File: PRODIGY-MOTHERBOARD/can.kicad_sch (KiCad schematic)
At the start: 10 parts, among them U4 TJA1051T-E

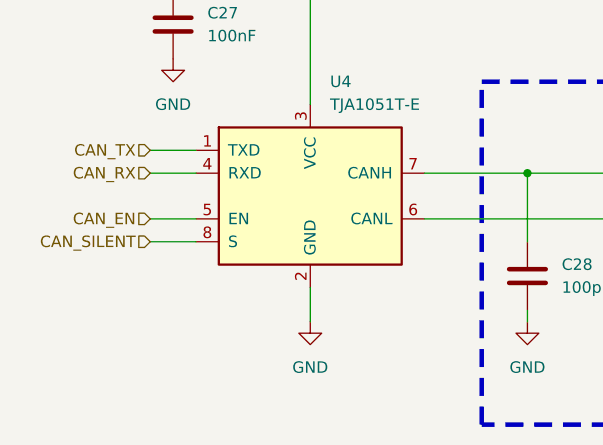
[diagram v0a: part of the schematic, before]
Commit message: MBT Schematic improved
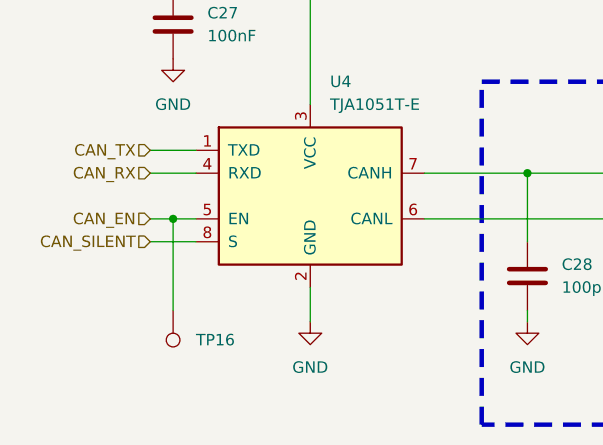
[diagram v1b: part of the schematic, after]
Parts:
- added TP16: ~, TestPoint:TestPoint_Pad_D3.0mm, symbol Connector:TestPoint
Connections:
- net CAN_EN: now also TP16.1
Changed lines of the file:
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@@
+	)
+	(junction
+		(at 95.25 91.44)
+		(diameter 0)
+		(color 0 0 0 0)
 	)
 	(junction
@@
 	(wire
 		(pts
+			(xy 95.25 91.44) (xy 95.25 101.6)
+		)
+		(stroke
+			(width 0)
+			(type default)
+		)
+	)
+	(wire
+		(pts
 			(xy 210.82 80.01) (xy 248.92 80.01)
 		)
@@
 	(wire
 		(pts
+			(xy 95.25 91.44) (xy 97.79 91.44)
+		)
+		(stroke
+			(width 0)
+			(type default)
+		)
+	)
+	(wire
+		(pts
 			(xy 110.49 66.04) (xy 110.49 78.74)
 		)
@@
 	(wire
 		(pts
-			(xy 92.71 91.44) (xy 97.79 91.44)
+			(xy 92.71 91.44) (xy 95.25 91.44)
 		)
 		(stroke
@@
 					(unit 1)
 				)
+			)
+		)
+	)
+	(symbol
+		(lib_id "Connector:TestPoint")
+		(at 95.25 101.6 180)
+		(unit 1)
+		(exclude_from_sim no)
+		(in_bom no)
+		(on_board yes)
+		(dnp no)
+		(fields_autoplaced yes)
+		(property "Reference" "TP16"
+			(at 97.79 104.9019 0)
+			(effects
+				(font
+					(size 1.27 1.27)
+				)
+				(justify right)
+			)
+		)
+		(property "Value" "~"
+			(at 92.71 102.997 0)
+			(effects
+				(font
+					(size 1.27 1.27)
+				)
+				(justify left)
+				(hide yes)
+			)
+		)
+		(property "Footprint" "TestPoint:TestPoint_Pad_D3.0mm"
+			(at 90.17 101.6 0)
+			(effects
+				(font
+					(size 1.27 1.27)
+				)
+				(hide yes)
+			)
+		)
+		(property "Datasheet" "~"
+			(at 90.17 101.6 0)
+			(effects
+				(font
+					(size 1.27 1.27)
+				)
+				(hide yes)
+			)
+		)
+		(property "Description" ""
+			(at 95.25 101.6 0)
+			(effects
+				(font
+					(size 1.27 1.27)
+				)
+				(hide yes)
+			)
+		)
+		(pin "1"
+		)
+		(instances
+			(project "PRODIGY-MOTHERBOARD"
+				(path "/f1c25860-8989-4190-bd24-2491d23ca7d9/cf0d8bf1-4632-49df-9398-b3de35528304"
+					(reference "TP16")
+					(unit 1)
+				)

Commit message: schematic v0.2 finalized
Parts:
- added FID11, FID12: Fiducial, symbol Mechanical:Fiducial
- renumbered C27 to C26, C28 to C27, C29 to C28, C30 to C29, C31 to C30, C32 to C31, TP16 to TP9
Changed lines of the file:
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@@
 		(dnp no)
 		(fields_autoplaced yes)
-		(property "Reference" "#PWR064"
+		(property "Reference" "#PWR067"
 			(at 220.98 105.41 0)
 			(effects
@@
 			(project "PRODIGY-MOTHERBOARD"
 				(path "/f1c25860-8989-4190-bd24-2491d23ca7d9/cf0d8bf1-4632-49df-9398-b3de35528304"
-					(reference "#PWR064")
+					(reference "#PWR067")
 					(unit 1)
 				)
@@
 		(dnp no)
 		(fields_autoplaced yes)
-		(property "Reference" "TP16"
+		(property "Reference" "TP9"
 			(at 97.79 104.9019 0)
 			(effects
@@
 			(project "PRODIGY-MOTHERBOARD"
 				(path "/f1c25860-8989-4190-bd24-2491d23ca7d9/cf0d8bf1-4632-49df-9398-b3de35528304"
-					(reference "TP16")
+					(reference "TP9")
 					(unit 1)
 				)
@@
 		(dnp no)
 		(fields_autoplaced yes)
-		(property "Reference" "C29"
+		(property "Reference" "C28"
 			(at 152.4 96.5199 0)
 			(effects
@@
 			(project "PRODIGY-MOTHERBOARD"
 				(path "/f1c25860-8989-4190-bd24-2491d23ca7d9/cf0d8bf1-4632-49df-9398-b3de35528304"
-					(reference "C29")
+					(reference "C28")
 					(unit 1)
 				)
@@
 		(dnp no)
 		(fields_autoplaced yes)
-		(property "Reference" "#PWR063"
+		(property "Reference" "#PWR066"
 			(at 180.34 109.22 0)
 			(effects
@@
 			(project "PRODIGY-MOTHERBOARD"
 				(path "/f1c25860-8989-4190-bd24-2491d23ca7d9/cf0d8bf1-4632-49df-9398-b3de35528304"
-					(reference "#PWR063")
+					(reference "#PWR066")
 					(unit 1)
 				)
@@
 		(dnp no)
 		(fields_autoplaced yes)
-		(property "Reference" "#PWR061"
+		(property "Reference" "#PWR064"
 			(at 148.59 109.22 0)
 			(effects
@@
 			(project "PRODIGY-MOTHERBOARD"
 				(path "/f1c25860-8989-4190-bd24-2491d23ca7d9/cf0d8bf1-4632-49df-9398-b3de35528304"
-					(reference "#PWR061")
+					(reference "#PWR064")
+					(unit 1)
+				)
+			)
+		)
+	)
+	(symbol
+		(lib_id "Mechanical:Fiducial")
+		(at 133.35 121.92 0)
+		(unit 1)
+		(exclude_from_sim no)
+		(in_bom yes)
+		(on_board yes)
+		(dnp no)
+		(fields_autoplaced yes)
+		(property "Reference" "FID11"
+			(at 135.89 120.6499 0)
+			(effects
+				(font
+					(size 1.27 1.27)
+				)
+				(justify left)
+			)
+		)
+		(property "Value" "Fiducial"
+			(at 135.89 123.1899 0)
+			(effects
+				(font
+					(size 1.27 1.27)
+				)
+				(justify left)
+			)
+		)
+		(property "Footprint" ""
+			(at 133.35 121.92 0)
+			(effects
+				(font
+					(size 1.27 1.27)
+				)
+				(hide yes)
+			)
+		)
+		(property "Datasheet" "~"
+			(at 133.35 121.92 0)
+			(effects
+				(font
+					(size 1.27 1.27)
+				)
+				(hide yes)
+			)
+		)
+		(property "Description" "Fiducial Marker"
+			(at 133.35 121.92 0)
+			(effects
+				(font
+					(size 1.27 1.27)
+				)
+				(hide yes)
+			)
+		)
+		(instances
+			(project "PRODIGY-MOTHERBOARD"
+				(path "/f1c25860-8989-4190-bd24-2491d23ca7d9/cf0d8bf1-4632-49df-9398-b3de35528304"
+					(reference "FID11")
 					(unit 1)
 				)
@@
 		(dnp no)
 		(fields_autoplaced yes)
-		(property "Reference" "C32"
+		(property "Reference" "C31"
 			(at 224.79 91.4399 0)
 			(effects
@@
 			(project "PRODIGY-MOTHERBOARD"
 				(path "/f1c25860-8989-4190-bd24-2491d23ca7d9/cf0d8bf1-4632-49df-9398-b3de35528304"
-					(reference "C32")
+					(reference "C31")
 					(unit 1)
 				)
@@
 		(dnp no)
 		(fields_autoplaced yes)
-		(property "Reference" "#PWR062"
+		(property "Reference" "#PWR065"
 			(at 166.37 109.22 0)
 			(effects
@@
 			(project "PRODIGY-MOTHERBOARD"
 				(path "/f1c25860-8989-4190-bd24-2491d23ca7d9/cf0d8bf1-4632-49df-9398-b3de35528304"
-					(reference "#PWR062")
+					(reference "#PWR065")
 					(unit 1)
 				)
@@
 		(dnp no)
 		(fields_autoplaced yes)
-		(property "Reference" "C28"
+		(property "Reference" "C27"
 			(at 138.43 96.5199 0)
 			(effects
@@
 			(project "PRODIGY-MOTHERBOARD"
 				(path "/f1c25860-8989-4190-bd24-2491d23ca7d9/cf0d8bf1-4632-49df-9398-b3de35528304"
-					(reference "C28")
+					(reference "C27")
 					(unit 1)
 				)
@@
 		(dnp no)
 		(fields_autoplaced yes)
-		(property "Reference" "#PWR060"
+		(property "Reference" "#PWR063"
 			(at 134.62 109.22 0)
 			(effects
@@
 			(project "PRODIGY-MOTHERBOARD"
 				(path "/f1c25860-8989-4190-bd24-2491d23ca7d9/cf0d8bf1-4632-49df-9398-b3de35528304"
-					(reference "#PWR060")
+					(reference "#PWR063")
+					(unit 1)
+				)
+			)
+		)
+	)
+	(symbol
+		(lib_id "Mechanical:Fiducial")
+		(at 133.35 127 0)
+		(unit 1)
+		(exclude_from_sim no)
+		(in_bom yes)
+		(on_board yes)
+		(dnp no)
+		(fields_autoplaced yes)
+		(property "Reference" "FID12"
+			(at 135.89 125.7299 0)
+			(effects
+				(font
+					(size 1.27 1.27)
+				)
+				(justify left)
+			)
+		)
+		(property "Value" "Fiducial"
+			(at 135.89 128.2699 0)
+			(effects
+				(font
+					(size 1.27 1.27)
+				)
+				(justify left)
+			)
+		)
+		(property "Footprint" ""
+			(at 133.35 127 0)
+			(effects
+				(font
+					(size 1.27 1.27)
+				)
+				(hide yes)
+			)
+		)
+		(property "Datasheet" "~"
+			(at 133.35 127 0)
+			(effects
+				(font
+					(size 1.27 1.27)
+				)
+				(hide yes)
+			)
+		)
+		(property "Description" "Fiducial Marker"
+			(at 133.35 127 0)
+			(effects
+				(font
+					(size 1.27 1.27)
+				)
+				(hide yes)
+			)
+		)
+		(instances
+			(project "PRODIGY-MOTHERBOARD"
+				(path "/f1c25860-8989-4190-bd24-2491d23ca7d9/cf0d8bf1-4632-49df-9398-b3de35528304"
+					(reference "FID12")
 					(unit 1)
 				)
@@
 		(dnp no)
 		(fields_autoplaced yes)
-		(property "Reference" "C31"
+		(property "Reference" "C30"
 			(at 184.15 96.5199 0)
 			(effects
@@
 			(project "PRODIGY-MOTHERBOARD"
 				(path "/f1c25860-8989-4190-bd24-2491d23ca7d9/cf0d8bf1-4632-49df-9398-b3de35528304"
-					(reference "C31")
+					(reference "C30")
 					(unit 1)
 				)
@@
 		(dnp no)
 		(fields_autoplaced yes)
-		(property "Reference" "C30"
+		(property "Reference" "C29"
 			(at 170.18 96.5199 0)
 			(effects
@@
 			(project "PRODIGY-MOTHERBOARD"
 				(path "/f1c25860-8989-4190-bd24-2491d23ca7d9/cf0d8bf1-4632-49df-9398-b3de35528304"
-					(reference "C30")
+					(reference "C29")
 					(unit 1)
 				)
@@
 		(dnp no)
 		(fields_autoplaced yes)
-		(property "Reference" "C27"
+		(property "Reference" "C26"
 			(at 99.06 68.5799 0)
 			(effects
@@
 			(project "PRODIGY-MOTHERBOARD"
 				(path "/f1c25860-8989-4190-bd24-2491d23ca7d9/cf0d8bf1-4632-49df-9398-b3de35528304"
-					(reference "C27")
+					(reference "C26")
 					(unit 1)
 				)
@@
 		(dnp no)
 		(fields_autoplaced yes)
-		(property "Reference" "#PWR057"
+		(property "Reference" "#PWR060"
 			(at 95.25 80.01 0)
 			(effects
@@
 			(project "PRODIGY-MOTHERBOARD"
 				(path "/f1c25860-8989-4190-bd24-2491d23ca7d9/cf0d8bf1-4632-49df-9398-b3de35528304"
-					(reference "#PWR057")
+					(reference "#PWR060")
 					(unit 1)
 				)
@@
 		(dnp no)
 		(fields_autoplaced yes)
-		(property "Reference" "#PWR059"
+		(property "Reference" "#PWR062"
 			(at 110.49 109.22 0)
 			(effects
@@
 			(project "PRODIGY-MOTHERBOARD"
 				(path "/f1c25860-8989-4190-bd24-2491d23ca7d9/cf0d8bf1-4632-49df-9398-b3de35528304"
-					(reference "#PWR059")
+					(reference "#PWR062")
 					(unit 1)
 				)
@@
 		(dnp no)
 		(fields_autoplaced yes)
-		(property "Reference" "#PWR058"
+		(property "Reference" "#PWR061"
 			(at 110.49 68.58 0)
 			(effects
@@
 			(project "PRODIGY-MOTHERBOARD"
 				(path "/f1c25860-8989-4190-bd24-2491d23ca7d9/cf0d8bf1-4632-49df-9398-b3de35528304"
-					(reference "#PWR058")
-					(unit 1)
-				)
+					(reference "#PWR061")
+					(unit 1)
+				)

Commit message: Motherboard footprints assigned.
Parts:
- C27, C28, C29, C30, C31: footprint (none) -> Capacitor_SMD:C_0603_1608Metric
- FID11, FID12: footprint (none) -> Fiducial:Fiducial_1mm_Mask3mm
- R23, R24: footprint Resistor_SMD:R_1206_3216Metric -> Resistor_SMD:R_0805_2012Metric

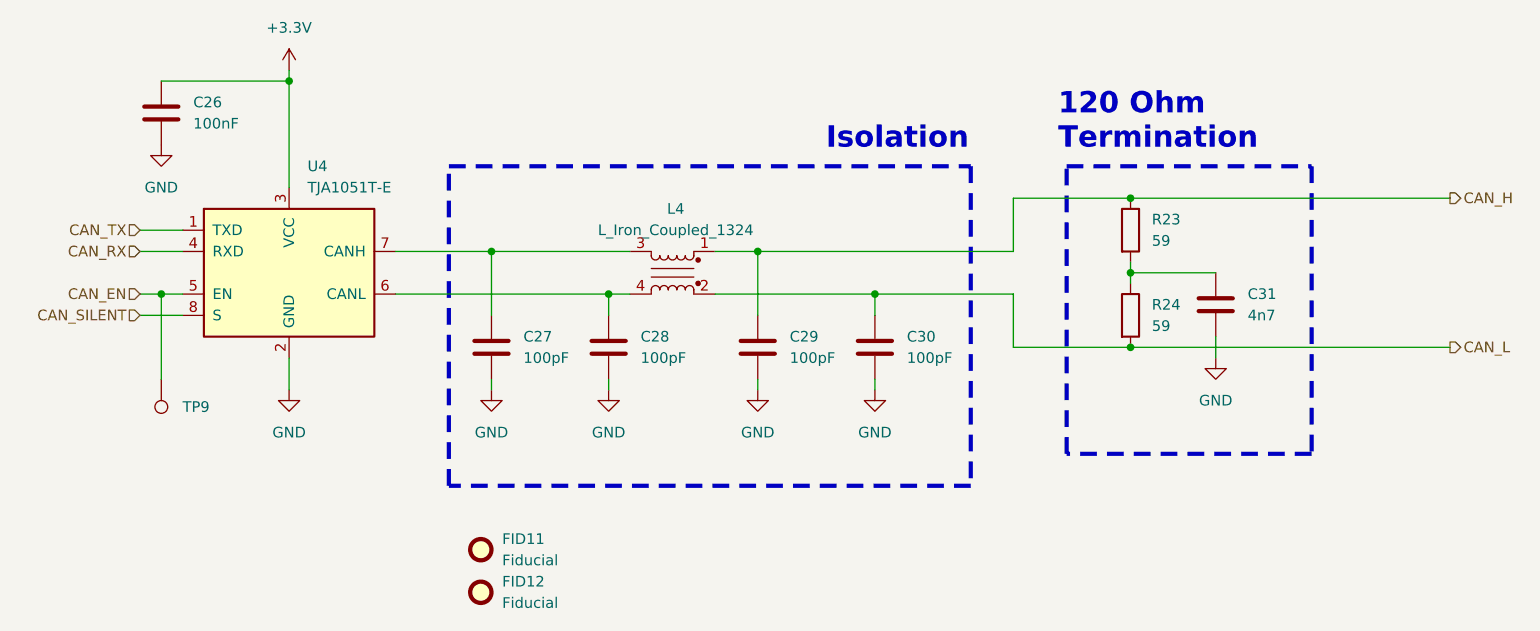
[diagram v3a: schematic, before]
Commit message: finished motherboard bom and updated footprints
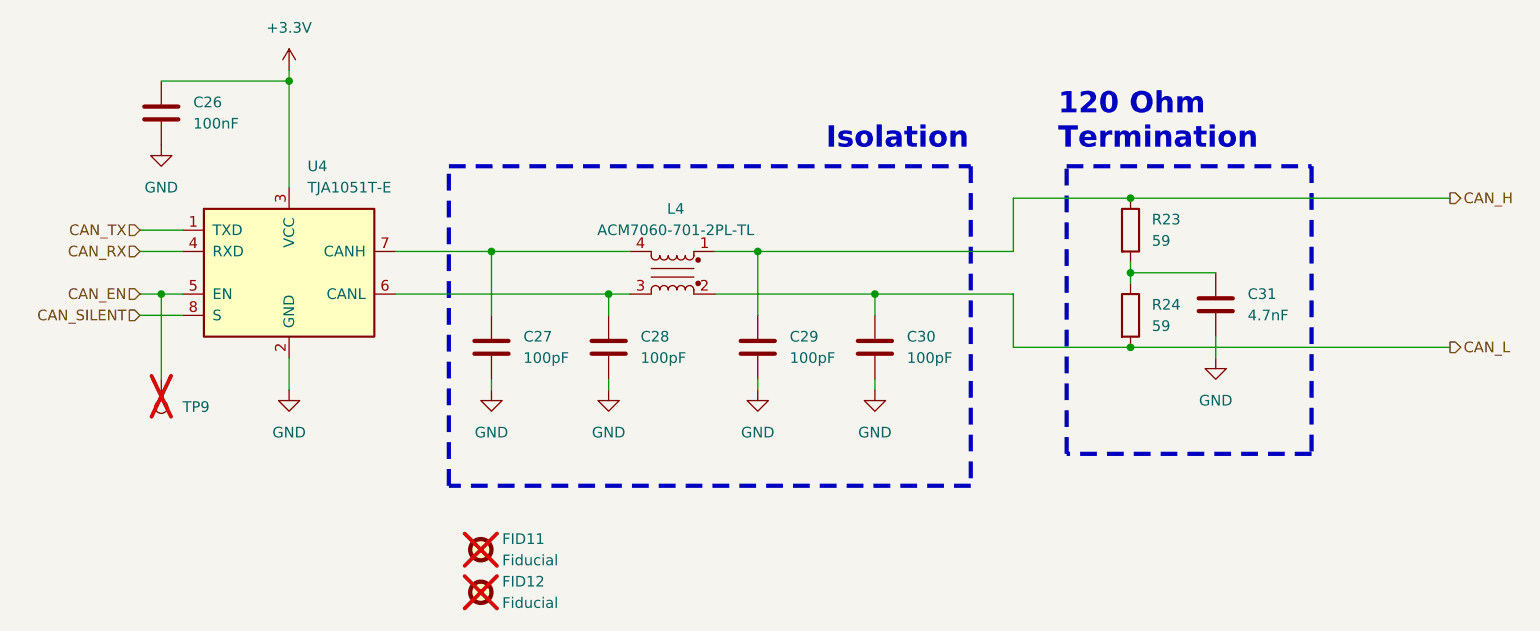
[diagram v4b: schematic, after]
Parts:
- removed L4: L_Iron_Coupled_1324, Inductor_SMD:L_CommonModeChoke_TDK_ACM7060, symbol Device:L_Iron_Coupled_1324
- added L4: ACM7060-701-2PL-TL, Inductor_SMD:L_CommonModeChoke_TDK_ACM7060, symbol Device:L_Iron_Coupled_1423
- C26: TME (none) -> CL10B104KB8NNNC
- C27, C28, C29, C30: TME (none) -> 0603N101J500CT
- C31: value 4n7 -> 4.7nF; TME (none) -> 06031C472KAT2A
- FID11, FID12, TP9: now not fitted
- R23, R24: footprint Resistor_SMD:R_0805_2012Metric -> Resistor_SMD:R_0603_1608Metric; TME (none) -> ERA3AEB59R0V
- U4: TME (none) -> TJA1051T/E.118
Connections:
- net CAN_H: now also L4.1
- net CAN_L: now also L4.2
- net at C28.1, U4.6 (CANL): now also L4.3
- net at C27.1, U4.7 (CANH): now also L4.4
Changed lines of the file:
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@@
+	)
+	(symbol
+		(lib_id "Device:L_Iron_Coupled_1423")
+		(at 156.21 88.9 0)
+		(mirror y)
+		(unit 1)
+		(exclude_from_sim no)
+		(in_bom yes)
+		(on_board yes)
+		(dnp no)
+		(fields_autoplaced yes)
+		(property "Reference" "L4"
+			(at 156.591 81.28 0)
+			(effects
+				(font
+					(size 1.27 1.27)
+				)
+			)
+		)
+		(property "Value" "ACM7060-701-2PL-TL"
+			(at 156.591 83.82 0)
+			(effects
+				(font
+					(size 1.27 1.27)
+				)
+			)
+		)
+		(property "Footprint" "Inductor_SMD:L_CommonModeChoke_TDK_ACM7060"
+			(at 156.21 88.9 0)
+			(effects
+				(font
+					(size 1.27 1.27)
+				)
+				(hide yes)
+			)
+		)
+		(property "Datasheet" "~"
+			(at 156.21 88.9 0)
+			(effects
+				(font
+					(size 1.27 1.27)
+				)
+				(hide yes)
+			)
+		)
+		(property "Description" "Coupled inductor with iron core"
+			(at 156.21 88.9 0)
+			(effects
+				(font
+					(size 1.27 1.27)
+				)
+				(hide yes)
+			)
+		)
+		(property "TME" "ACM7060-701-2PL-TL"
+			(at 156.21 88.9 0)
+			(effects
+				(font
+					(size 1.27 1.27)
+				)
+				(hide yes)
+			)
+		)
+		(pin "3"
+		)
+		(pin "2"
+		)
+		(pin "4"
+		)
+		(pin "1"
+		)
+		(instances
+			(project "PRODIGY-MOTHERBOARD"
+				(path "/f1c25860-8989-4190-bd24-2491d23ca7d9/cf0d8bf1-4632-49df-9398-b3de35528304"
+					(reference "L4")
+					(unit 1)
+				)
+			)
+		)
 	)
 	(symbol
@@
 		(in_bom no)
 		(on_board yes)
-		(dnp no)
+		(dnp yes)
 		(fields_autoplaced yes)
 		(property "Reference" "TP9"
@@
 			)
 		)
-		(property "TME" ""
+		(property "TME" "0603N101J500CT"
 			(at 148.59 97.79 0)
 			(effects
@@
 			)
 		)
-		(property "Footprint" "Resistor_SMD:R_0805_2012Metric"
+		(property "Footprint" "Resistor_SMD:R_0603_1608Metric"
 			(at 209.042 93.98 90)
 			(effects
@@
 			)
 		)
-		(property "TME" ""
+		(property "TME" "ERA3AEB59R0V"
 			(at 210.82 93.98 0)
 			(effects
@@
 		(in_bom yes)
 		(on_board yes)
-		(dnp no)
+		(dnp yes)
 		(fields_autoplaced yes)
 		(property "Reference" "FID11"
@@
 			)
 		)
-		(property "Value" "4n7"
+		(property "Value" "4.7nF"
 			(at 224.79 93.9799 0)
 			(effects
@@
 			)
 		)
-		(property "TME" ""
+		(property "TME" "06031C472KAT2A"
 			(at 220.98 92.71 0)
 			(effects
@@
 			)
 		)
-		(property "TME" ""
+		(property "TME" "0603N101J500CT"
 			(at 134.62 97.79 0)
 			(effects
@@
 		(in_bom yes)
 		(on_board yes)
-		(dnp no)
+		(dnp yes)
 		(fields_autoplaced yes)
 		(property "Reference" "FID12"
@@
 			)
 		)
-		(property "TME" ""
+		(property "TME" "0603N101J500CT"
 			(at 180.34 97.79 0)
 			(effects
@@
 			)
 		)
-		(property "TME" ""
+		(property "TME" "0603N101J500CT"
 			(at 166.37 97.79 0)
 			(effects
@@
 			)
 		)
-		(property "TME" ""
+		(property "TME" "CL10B104KB8NNNC  "
 			(at 95.25 69.85 0)
 			(effects
@@
 			)
 		)
-		(property "TME" ""
+		(property "TME" "TJA1051T/E.118"
 			(at 110.49 88.9 0)
 			(effects
@@
 				(path "/f1c25860-8989-4190-bd24-2491d23ca7d9/cf0d8bf1-4632-49df-9398-b3de35528304"
 					(reference "U4")
-					(unit 1)
-				)
-			)
-		)
-	)
-	(symbol
-		(lib_id "Device:L_Iron_Coupled_1324")
-		(at 156.21 88.9 0)
-		(mirror y)
-		(unit 1)
-		(exclude_from_sim no)
-		(in_bom yes)
-		(on_board yes)
-		(dnp no)
-		(fields_autoplaced yes)
-		(property "Reference" "L4"
-			(at 156.591 81.28 0)
-			(effects
-				(font
-					(size 1.27 1.27)
-				)
-			)
-		)
-		(property "Value" "L_Iron_Coupled_1324"
-			(at 156.591 83.82 0)
-			(effects
-				(font
-					(size 1.27 1.27)
-				)
-			)
-		)
-		(property "Footprint" "Inductor_SMD:L_CommonModeChoke_TDK_ACM7060"
-			(at 156.21 88.9 0)
-			(effects
-				(font
-					(size 1.27 1.27)
-				)
-				(hide yes)
-			)
-		)
-		(property "Datasheet" "~"
-			(at 156.21 88.9 0)
-			(effects
-				(font
-					(size 1.27 1.27)
-				)
-				(hide yes)
-			)
-		)
-		(property "Description" "Coupled inductor with iron core"
-			(at 156.21 88.9 0)
-			(effects
-				(font
-					(size 1.27 1.27)
-				)
-				(hide yes)
-			)
-		)
-		(property "MOUSER" ""
-			(at 156.21 88.9 0)
-			(effects
-				(font
-					(size 1.27 1.27)
-				)
-				(hide yes)
-			)
-		)
-		(property "Sim.Type" ""
-			(at 156.21 88.9 0)
-			(effects
-				(font
-					(size 1.27 1.27)
-				)
-				(hide yes)
-			)
-		)
-		(property "TME" ""
-			(at 156.21 88.9 0)
-			(effects
-				(font
-					(size 1.27 1.27)
-				)
-				(hide yes)
-			)
-		)
-		(pin "2"
-		)
-		(pin "4"
-		)
-		(pin "1"
-		)
-		(pin "3"
-		)
-		(instances
-			(project "PRODIGY-MOTHERBOARD"
-				(path "/f1c25860-8989-4190-bd24-2491d23ca7d9/cf0d8bf1-4632-49df-9398-b3de35528304"
-					(reference "L4")
 					(unit 1)
 				)
@@
 			)
 		)
-		(property "Footprint" "Resistor_SMD:R_0805_2012Metric"
+		(property "Footprint" "Resistor_SMD:R_0603_1608Metric"
 			(at 209.042 83.82 90)
 			(effects
@@
 			)
 		)
-		(property "TME" ""
+		(property "TME" "ERA3AEB59R0V"
 			(at 210.82 83.82 0)
 			(effects
